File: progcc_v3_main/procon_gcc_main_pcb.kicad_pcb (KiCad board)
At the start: 4 copper layers, 110.9 x 59.7 mm, 108 parts, among them J1 Rumble, J2 Rumble, J3 To Button Board, J4 Conn_01x06_Female, J5 Conn_01x02_Pin, J9 USB_C_Receptacle, P1 Endpoint, Q1 Q_PMOS_GDS, Q2 Q_NMOS_GSD, Q3 Q_NMOS_GSD, Q4 BSS138, Q5 BSS138, Q6 BSS138, SW1 GL18_SW, SW2 GL18_SW, SW3 TS-1187A-B-A-B, T1 36-8730, T2 36-8730, T3 36-8730, T4 36-8730, U1 GH39F (Hall SOT23), U10 MCP3002, U11 ST_LSM6, U2 GH39F (Hall SOT23), U3 GH39F (Hall SOT23), U4 GH39F (Hall SOT23), U5 ST_LSM6, U6 RP2040, U7 LP3986-33B3F, U8 MCP3002, U9 W25Q128JVS, Y1 Crystal_GND3

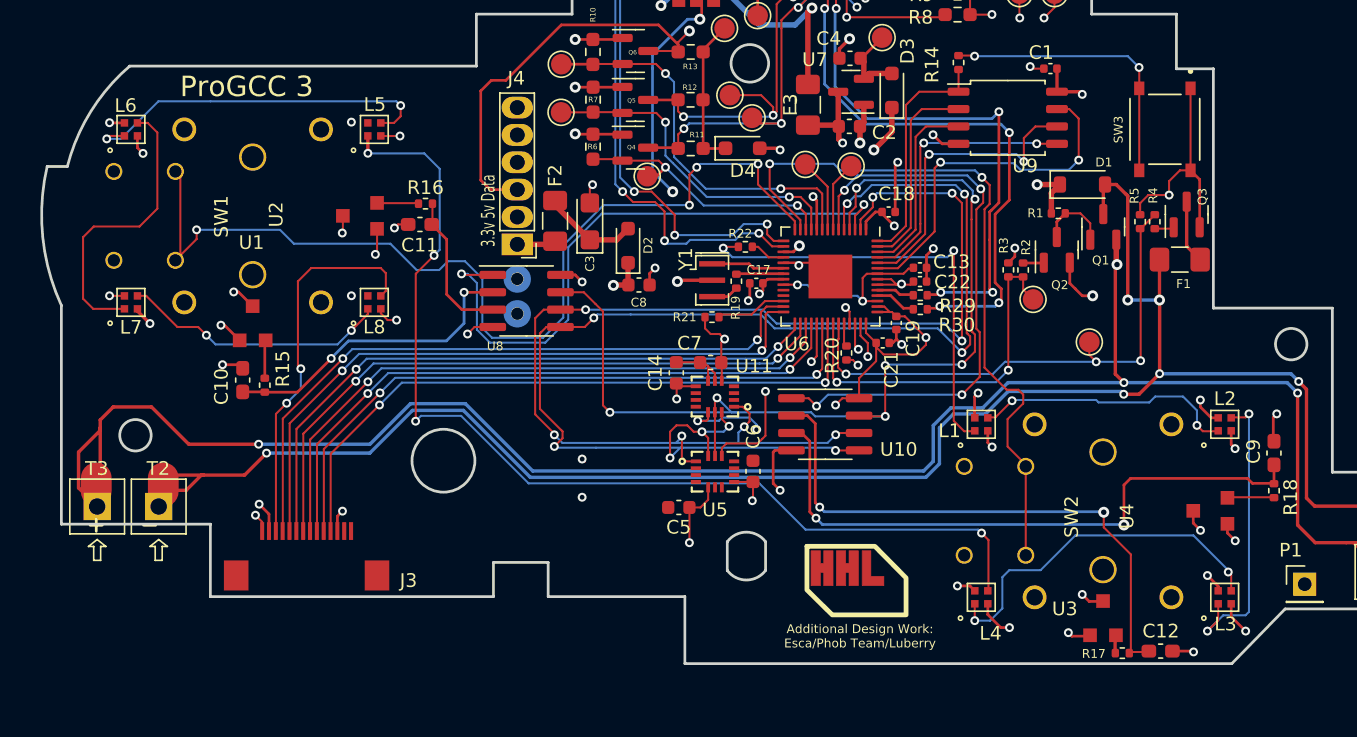
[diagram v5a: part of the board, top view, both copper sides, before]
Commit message: Fix Stick positions (More!)
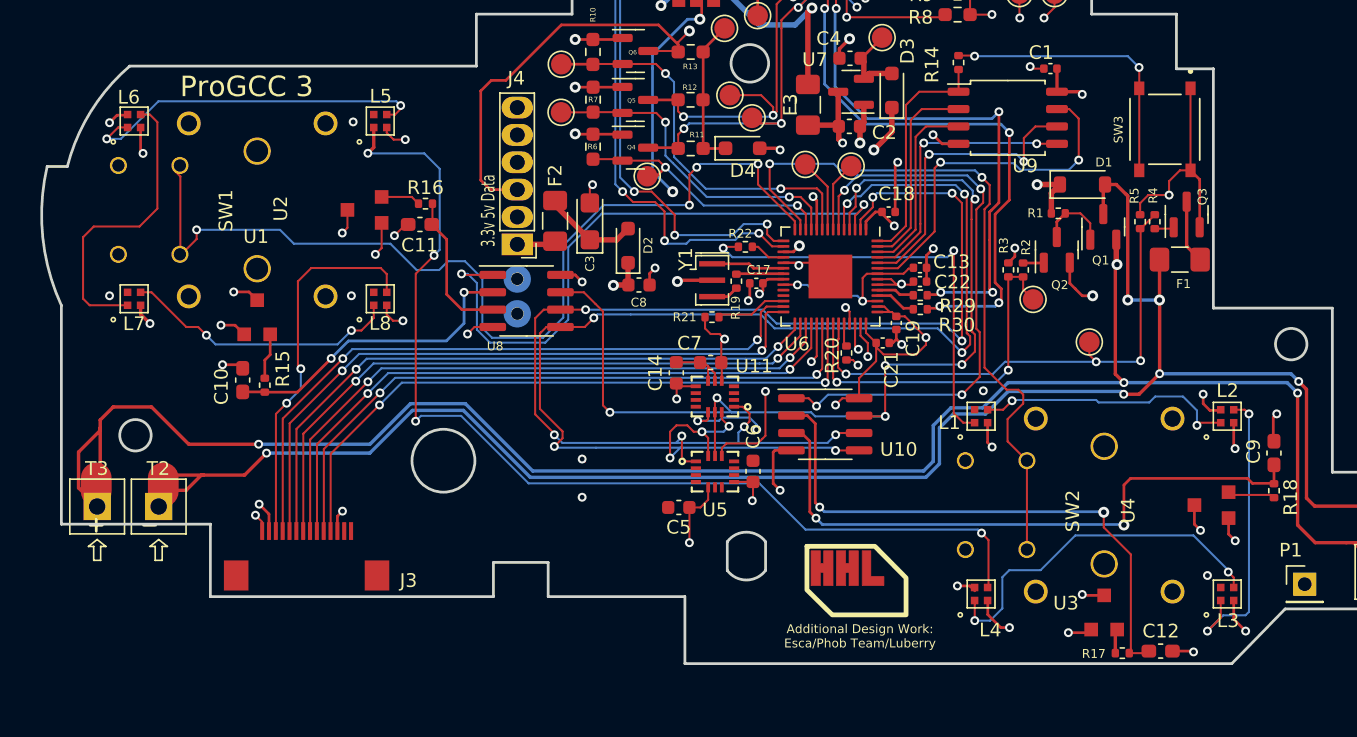
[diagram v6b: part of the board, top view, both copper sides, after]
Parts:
- moved L5 0.75 mm to (105.4, 111.9)
- moved L6 0.65 mm to (87.4, 111.9)
- moved L2 0.62 mm to (167.3, 133.5)
- moved L1 0.59 mm to (149.3, 133.5)
- moved SW1 0.55 mm to (96.4, 118.4)
- moved U1 0.55 mm to (96.4, 118.4)
- moved U2 0.55 mm to (96.4, 118.4)
- moved L8 0.51 mm to (105.4, 124.9)
- moved SW2 0.43 mm to (158.3, 140.0)
- moved U3 0.43 mm to (158.3, 140.0)
- moved U4 0.43 mm to (158.3, 140.0)
- moved L7 0.35 mm to (87.4, 124.9)
- moved L3 0.31 mm to (167.3, 146.5)
- moved L4 0.24 mm to (149.3, 146.5)
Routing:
- net +3V3: track 99.4 -> 103.5 mm
- net GND: track 109.7 -> 106.7 mm
- net Net-(L7-DOUT): track 19.6 -> 20.4 mm
- net SR_RGB: track 75.7 -> 76.5 mm
- net SL_RGB: track 32.8 -> 32.2 mm
- net Net-(L6-DOUT): track 21.4 -> 22.0 mm
- net Net-(L5-DOUT): track 26.6 -> 26.0 mm
- net Net-(U3-VOUT): track 1.25 -> 1.78 mm
